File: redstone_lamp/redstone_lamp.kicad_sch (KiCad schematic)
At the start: 71 parts, among them J1 1x4_Pogo, J2 1x4_Pogo, J3 1x4_Pogo, J4 1x4_Pogo, J5 1x4_Pogo, J6 1x4_Pogo, J7 1x4_Pogo, J8 1x4_Pogo, J9 2.54mm_ProgrammingPin, Q1 BC108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

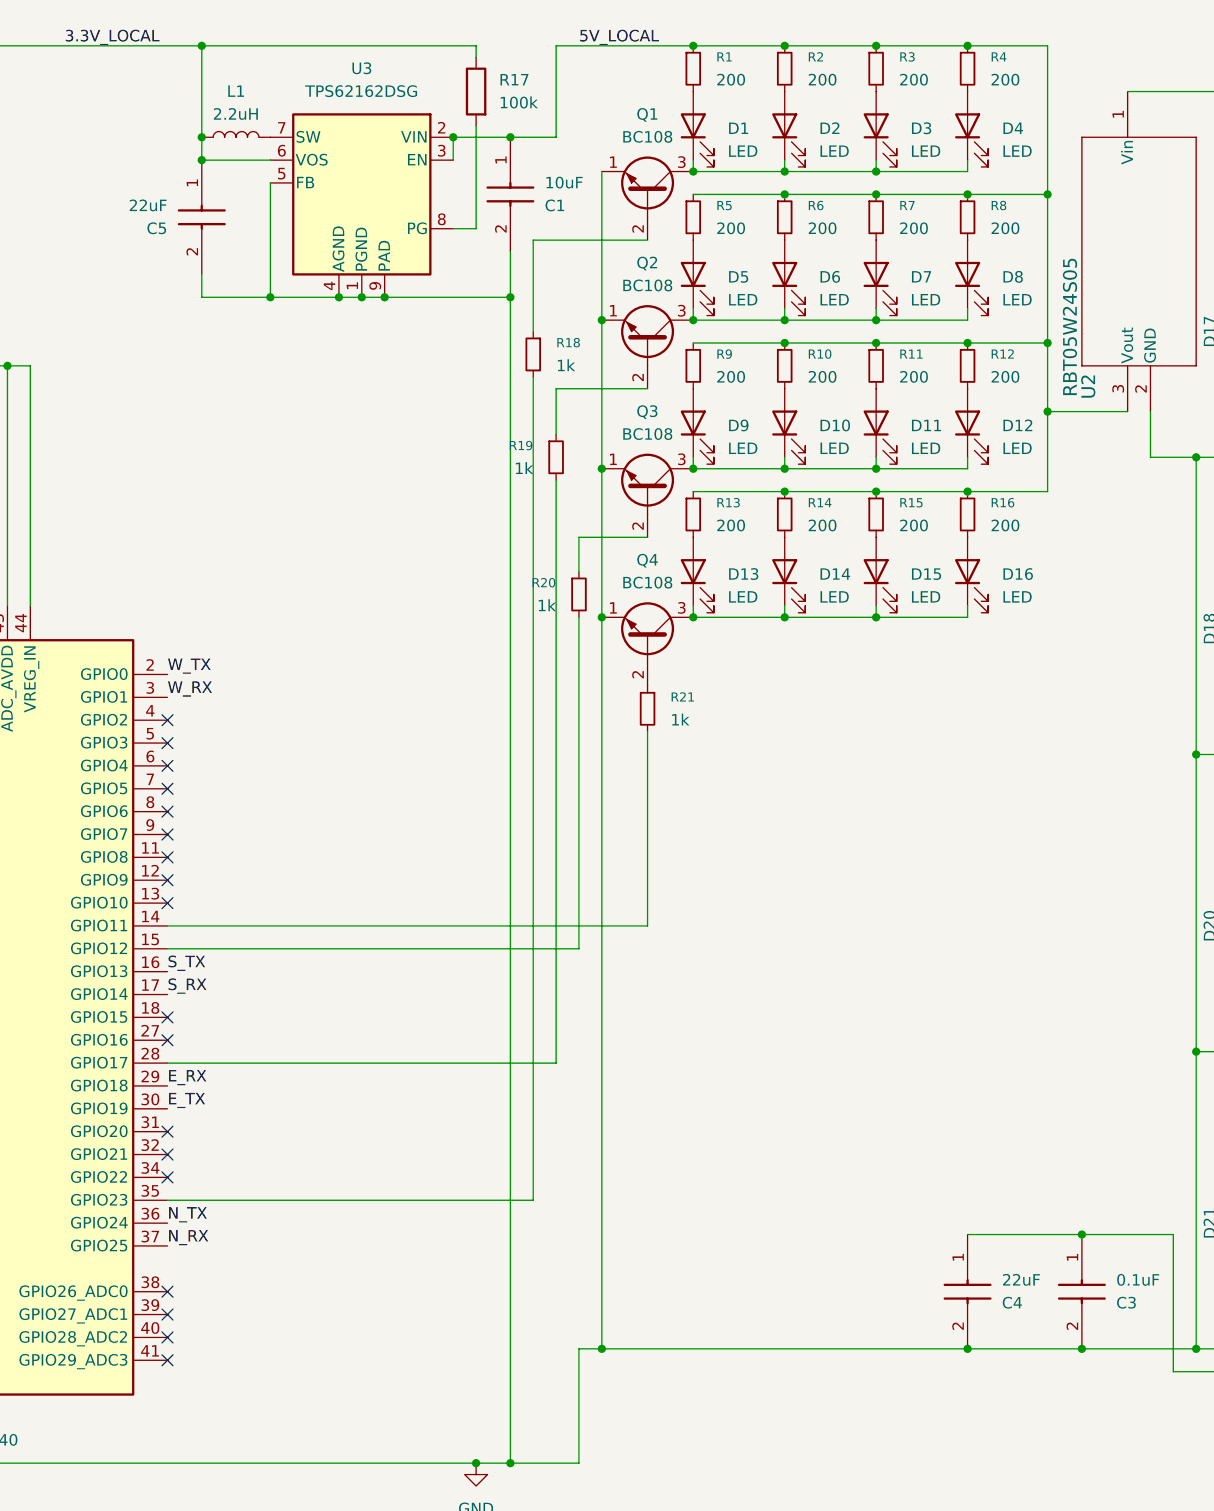
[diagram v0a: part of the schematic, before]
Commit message: remove all unecessary components in schematic
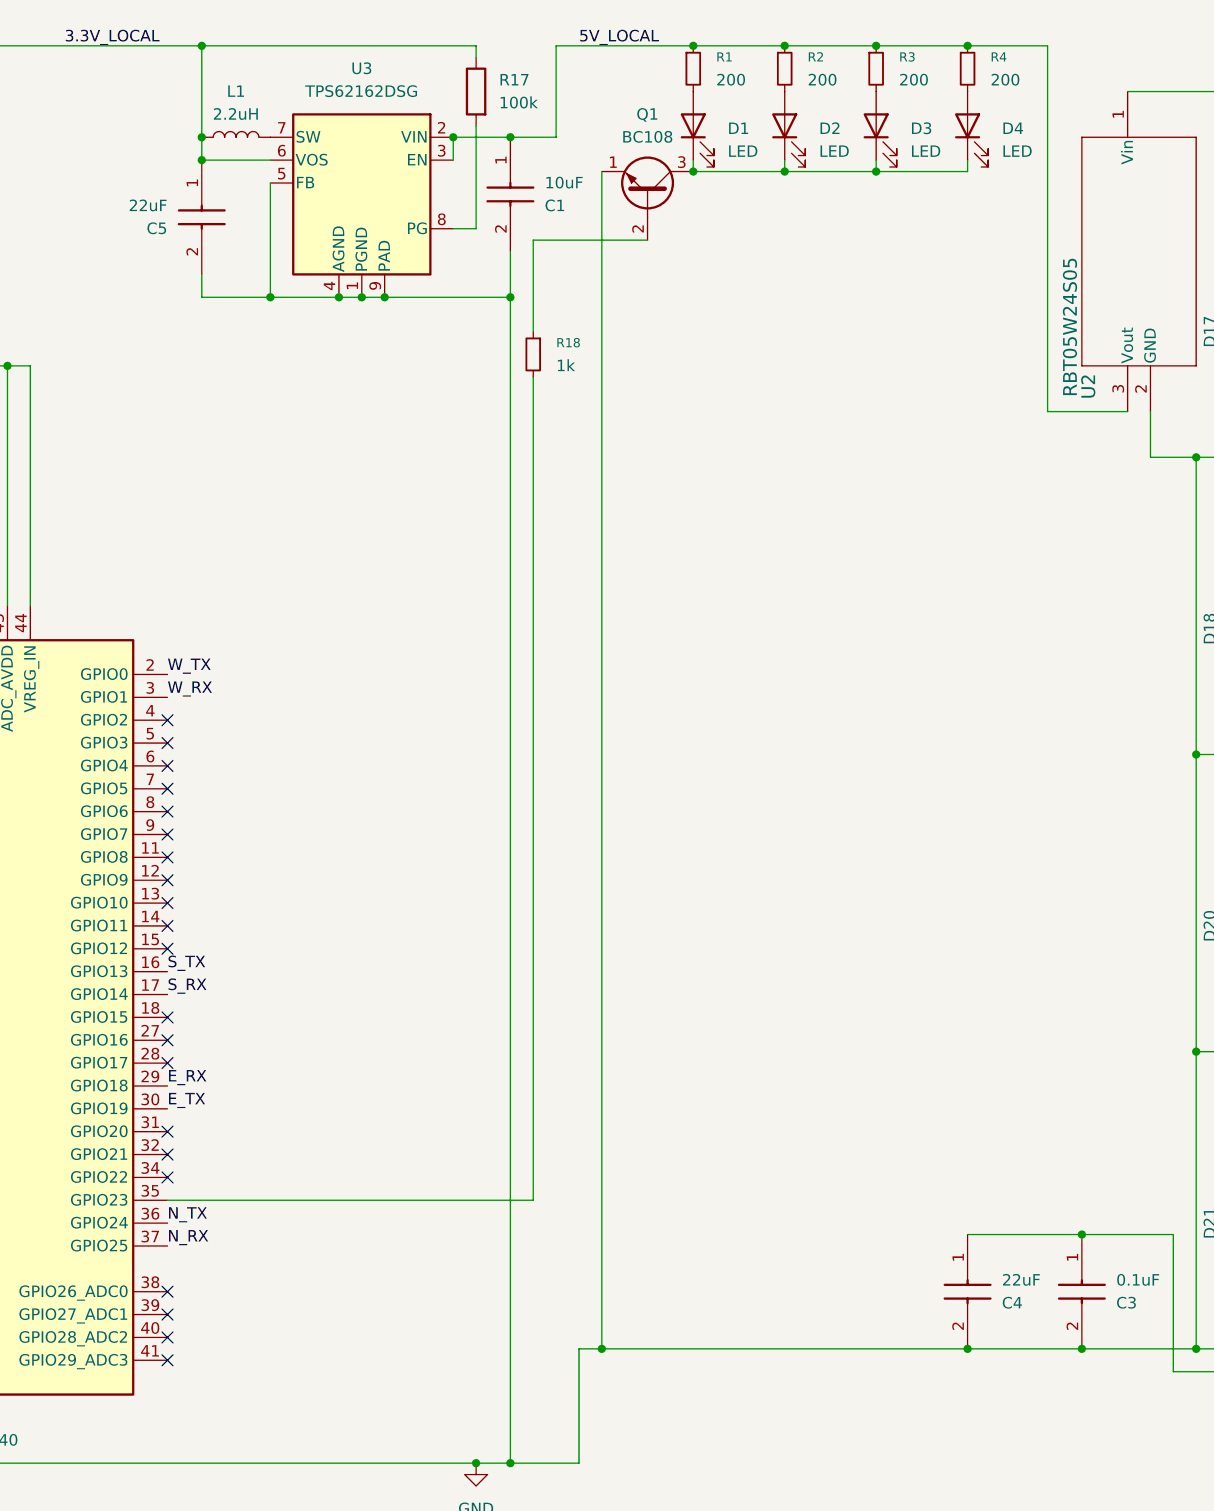
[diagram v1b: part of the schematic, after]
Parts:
- removed D10, D11, D12, D13, D14, D15, D16, D5, D6, D7, D8, D9: LED, SamacSys_Parts:LEDC1608X115N, symbol Device:LED
- removed Q2, Q3, Q4: BC108, Package_TO_SOT_THT:TO-18-3, symbol Transistor_BJT:BC108
- removed R10, R11, R12, R13, R14, R15, R16, R5, R6, R7, R8, R9: 200, SamacSys_Parts:CRCW1210200RJNEAIF, symbol Device:R_Small
- removed R19, R20, R21: 1k, SamacSys_Parts:ERJ-UP6D1001V, symbol Device:R_Small
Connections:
- no-connect marks 31 -> 34

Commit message: finalize redstone lamp design
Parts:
- removed R18: 1k, SamacSys_Parts:ERJ-UP6D1001V, symbol Device:R_Small
- added R5: 1k, SamacSys_Parts:ERJ-UP6D1001V, symbol Device:R
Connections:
- net E_RX: now also U1.30 (GPIO19); no longer U1.29 (GPIO18)
- net E_TX: now also U1.29 (GPIO18); no longer U1.30 (GPIO19)
- net at Q1.2 (B): now also R5.1
- net at U1.35 (GPIO23): now also R5.2

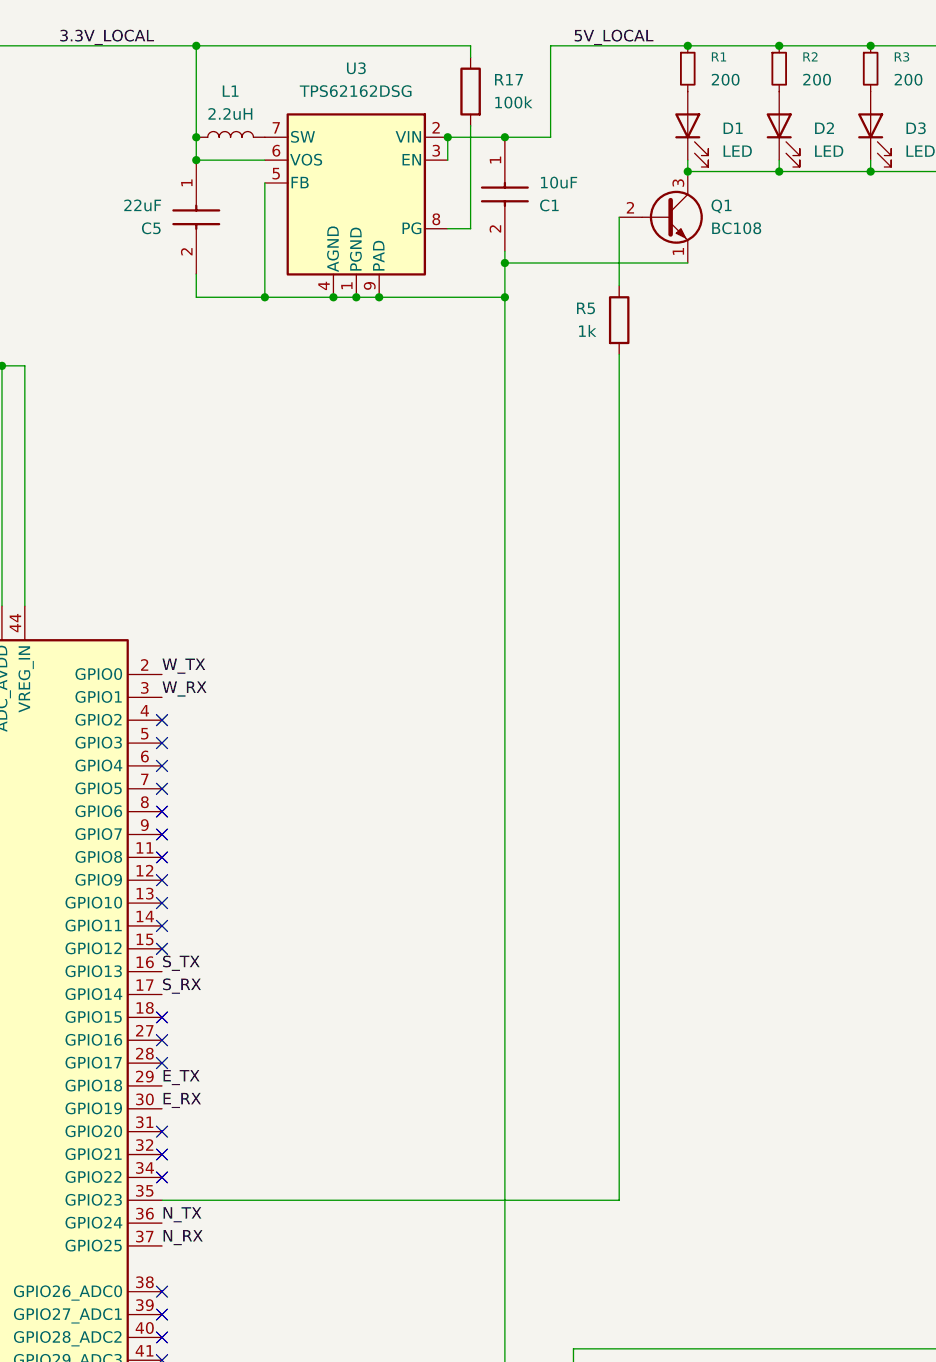
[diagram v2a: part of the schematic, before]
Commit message: switch redstone lamp transistor to mmbt3904
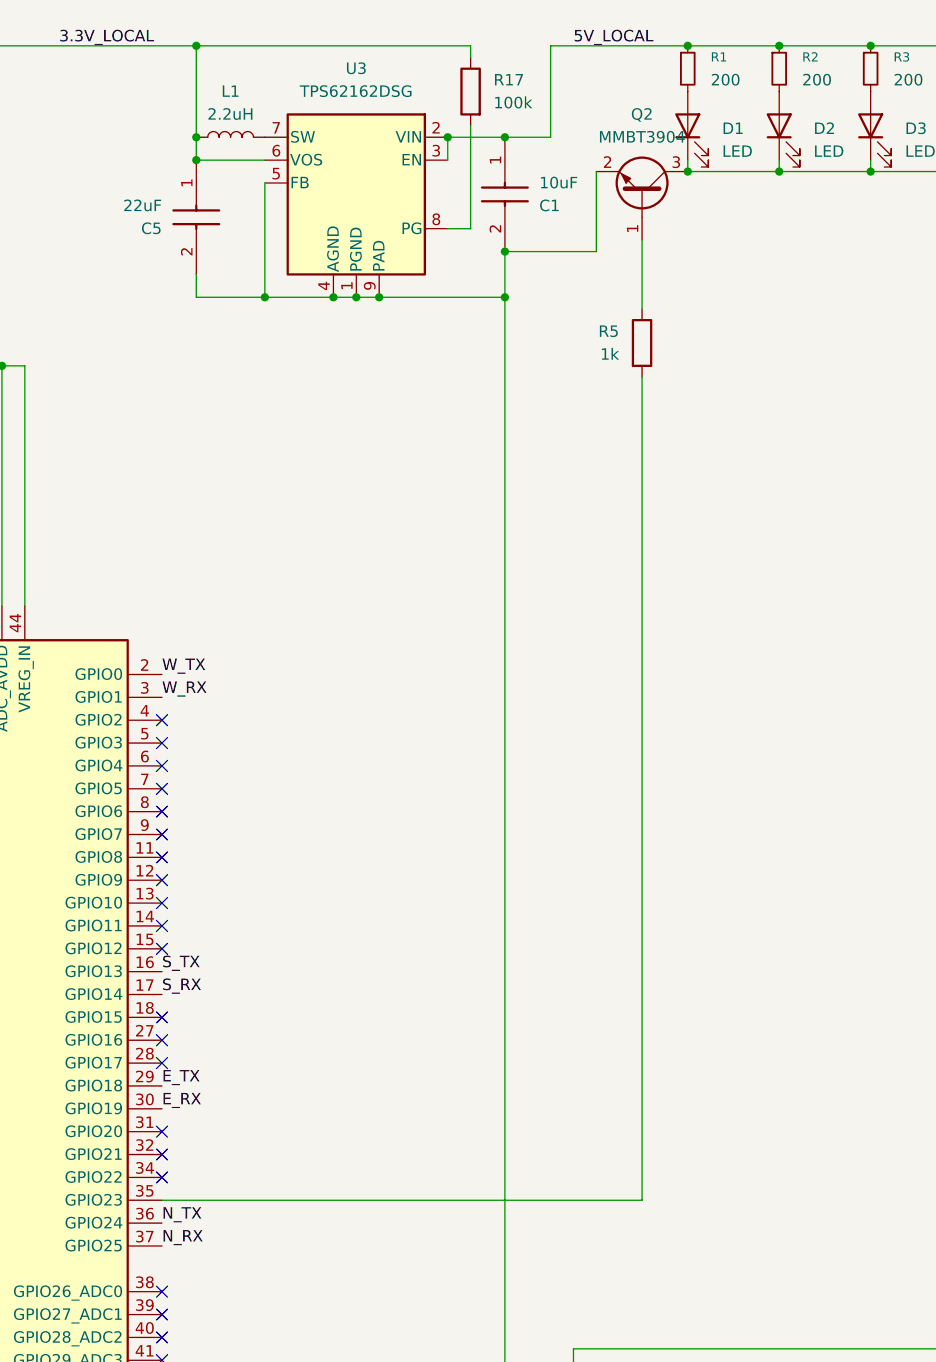
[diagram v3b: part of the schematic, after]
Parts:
- removed Q1: BC108, Package_TO_SOT_THT:TO-18-3, symbol Transistor_BJT:BC108
- added Q2: MMBT3904, Package_TO_SOT_SMD:SOT-23, symbol Transistor_BJT:MMBT3904
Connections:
- net GND: now also Q2.2 (E)
- net at D1.1 (K), D2.1 (K), D3.1 (K)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: now also Q2.3 (C)
- net at R5.1: now also Q2.1 (B)
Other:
- moved on the sheet: R5
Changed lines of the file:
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@@
 	)
 	(junction
-		(at 186.69 30.48)
-		(diameter 0)
-		(color 0 0 0 0)
-	)
-	(junction
 		(at 260.35 62.23)
 		(diameter 0)
@@
 	)
 	(junction
+		(at 166.37 39.37)
+		(diameter 0)
+		(color 0 0 0 0)
+	)
+	(junction
 		(at 257.81 125.73)
 		(diameter 0)
@@
 	)
 	(junction
+		(at 186.69 30.48)
+		(diameter 0)
+		(color 0 0 0 0)
+	)
+	(junction
 		(at 207.01 30.48)
 		(diameter 0)
@@
 	)
 	(junction
-		(at 166.37 40.64)
-		(diameter 0)
-		(color 0 0 0 0)
-	)
-	(junction
 		(at 166.37 44.45)
 		(diameter 0)
@@
 	(wire
 		(pts
-			(xy 166.37 39.37) (xy 166.37 40.64)
-		)
-		(stroke
-			(width 0)
-			(type default)
-			(color 0 0 0 1)
-		)
-	)
-	(wire
-		(pts
 			(xy 48.26 93.98) (xy 62.23 93.98)
 		)
@@
 	(wire
 		(pts
-			(xy 179.07 35.56) (xy 179.07 43.18)
+			(xy 181.61 38.1) (xy 181.61 45.72)
 		)
 		(stroke
@@
 	(wire
 		(pts
-			(xy 179.07 50.8) (xy 179.07 144.78)
+			(xy 181.61 53.34) (xy 181.61 144.78)
 		)
 		(stroke
@@
 	(wire
 		(pts
-			(xy 179.07 144.78) (xy 128.27 144.78)
+			(xy 181.61 144.78) (xy 128.27 144.78)
 		)
 		(stroke
@@
 	(wire
 		(pts
-			(xy 166.37 40.64) (xy 166.37 44.45)
+			(xy 166.37 39.37) (xy 166.37 44.45)
 		)
 		(stroke
@@
 	(wire
 		(pts
+			(xy 176.53 39.37) (xy 166.37 39.37)
+		)
+		(stroke
+			(width 0)
+			(type default)
+		)
+	)
+	(wire
+		(pts
 			(xy 240.03 163.83) (xy 240.03 148.59)
 		)
@@
 	(wire
 		(pts
-			(xy 166.37 40.64) (xy 186.69 40.64)
-		)
-		(stroke
-			(width 0)
-			(type default)
-		)
-	)
-	(wire
-		(pts
 			(xy 82.55 21.59) (xy 82.55 45.72)
 		)
@@
 	(wire
 		(pts
+			(xy 176.53 30.48) (xy 176.53 39.37)
+		)
+		(stroke
+			(width 0)
+			(type default)
+		)
+	)
+	(wire
+		(pts
 			(xy 77.47 173.99) (xy 102.87 173.99)
 		)
@@
 	(symbol
 		(lib_id "Device:R")
-		(at 179.07 46.99 0)
+		(at 181.61 49.53 0)
 		(unit 1)
 		(exclude_from_sim no)
@@
 		(dnp no)
 		(property "Reference" "R5"
-			(at 176.53 45.7199 0)
+			(at 179.07 48.2599 0)
 			(effects
 				(font
@@
 		)
 		(property "Value" "1k"
-			(at 176.53 48.2599 0)
+			(at 179.07 50.7999 0)
 			(effects
 				(font
@@
 		)
 		(property "Footprint" "SamacSys_Parts:ERJ-UP6D1001V"
-			(at 177.292 46.99 90)
+			(at 179.832 49.53 90)
 			(effects
 				(font
@@
 		)
 		(property "Datasheet" "~"
-			(at 179.07 46.99 0)
+			(at 181.61 49.53 0)
 			(effects
 				(font
@@
 		)
 		(property "Description" "Resistor"
-			(at 179.07 46.99 0)
+			(at 181.61 49.53 0)
 			(effects
 				(font
@@
 	)
 	(symbol
-		(lib_id "Transistor_BJT:BC108")
-		(at 184.15 35.56 0)
+		(lib_id "Transistor_BJT:MMBT3904")
+		(at 181.61 33.02 270)
+		(mirror x)
 		(unit 1)
 		(exclude_from_sim no)
@@
 		(dnp no)
 		(fields_autoplaced yes)
-		(property "Reference" "Q1"
-			(at 189.23 34.2899 0)
+		(property "Reference" "Q2"
+			(at 181.61 24.13 90)
 			(effects
 				(font
 					(size 1.27 1.27)
 				)
-				(justify left)
 			)
 		)
-		(property "Value" "BC108"
-			(at 189.23 36.8299 0)
+		(property "Value" "MMBT3904"
+			(at 181.61 26.67 90)
 			(effects
 				(font
 					(size 1.27 1.27)
 				)
-				(justify left)
 			)
 		)
-		(property "Footprint" "Package_TO_SOT_THT:TO-18-3"
-			(at 189.23 37.465 0)
+		(property "Footprint" "Package_TO_SOT_SMD:SOT-23"
+			(at 179.705 27.94 0)
 			(effects
 				(font
@@
 			)
 		)
-		(property "Datasheet" "http://www.b-kainka.de/Daten/Transistor/BC108.pdf"
-			(at 184.15 35.56 0)
+		(property "Datasheet" "https://www.onsemi.com/pdf/datasheet/pzt3904-d.pdf"
+			(at 181.61 33.02 0)
 			(effects
 				(font
@@
 			)
 		)
-		(property "Description" "0.1A Ic, 30V Vce, Low Noise General Purpose NPN Transistor, TO-18"
-			(at 184.15 35.56 0)
+		(property "Description" "0.2A Ic, 40V Vce, Small Signal NPN Transistor, SOT-23"
+			(at 181.61 33.02 0)
 			(effects
 				(font
@@
 			)
 		)
+		(pin "3"
+		)
 		(pin "2"
 		)
 		(pin "1"
 		)
-		(pin "3"
-		)
 		(instances
 			(project ""
 				(path "/bc70a981-f687-4b66-9b14-62168cfa8164"
-					(reference "Q1")
+					(reference "Q2")
 					(unit 1)
 				)
